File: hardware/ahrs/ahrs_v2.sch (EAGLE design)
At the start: 41 parts, among them J1 LINEAR_2_5040500291, J2 LINEAR_35040500391, J3 LINEAR_85040500891, U1 STM32G4_UFQFPN48_T1, U10 MCP2542FD, U11 LDFM33PUR, U2 LSM9DS1, X1 CRYSTAL_NX2016SA-24MHZ-EXS00A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

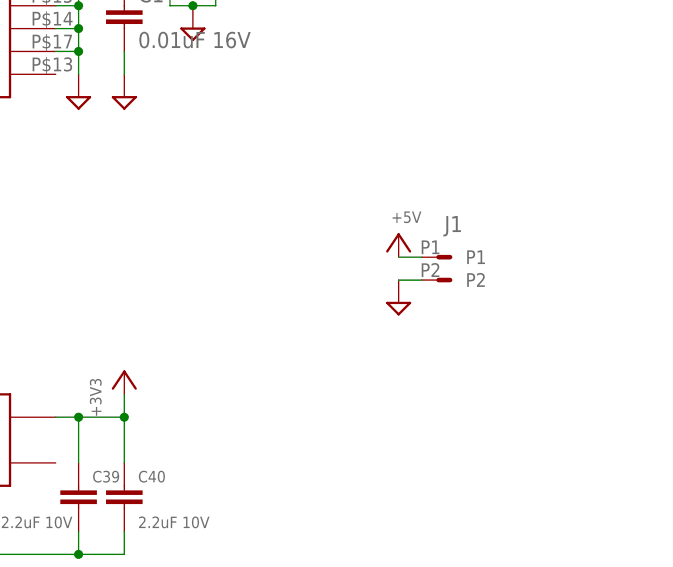
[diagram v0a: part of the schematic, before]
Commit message: Added TVS diode
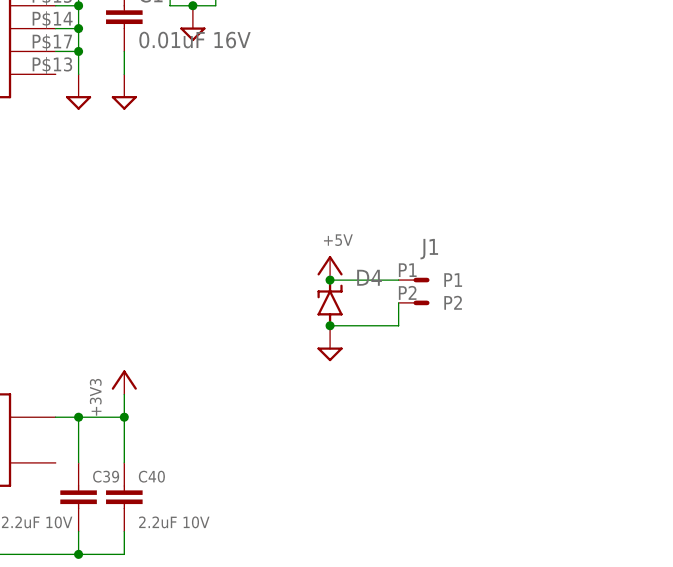
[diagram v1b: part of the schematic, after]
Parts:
- added D4: (no value), _T_rcl:TVS_SOD123
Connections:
- net +5V: now also D4.C
- net GND: now also D4.A
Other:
- moved on the sheet: J1
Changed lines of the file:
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@@
 <part name="R3" library="_T_rcl" library_urn="urn:adsk.eagle:library:19571919" deviceset="R" device="0603" package3d_urn="urn:adsk.eagle:package:19572012/3" value="22"/>
 <part name="GND13" library="_T_power" library_urn="urn:adsk.eagle:library:19572085" deviceset="GND" device=""/>
+<part name="D4" library="_T_rcl" library_urn="urn:adsk.eagle:library:19571919" deviceset="TVS" device="_SOD123" package3d_urn="urn:adsk.eagle:package:20295471/2"/>
 </parts>
 <sheets>
@@
 <attribute name="VALUE" x="70.8406" y="70.0786" size="2.0828" layer="96" ratio="6" rot="SR0"/>
 </instance>
-<instance part="J1" gate="G$1" x="251.46" y="91.44" smashed="yes" grouprefs="POWER">
-<attribute name="NAME" x="248.92" y="94.234" size="1.778" layer="95"/>
-</instance>
-<instance part="GND12" gate="G$1" x="243.84" y="86.36" smashed="yes" grouprefs="POWER"/>
-<instance part="+5V2" gate="G$1" x="243.84" y="93.98" smashed="yes" grouprefs="POWER">
-<attribute name="VALUE" x="246.38" y="96.52" size="1.27" layer="96" rot="R180"/>
+<instance part="J1" gate="G$1" x="248.92" y="88.9" smashed="yes" grouprefs="POWER">
+<attribute name="NAME" x="246.38" y="91.694" size="1.778" layer="95"/>
+</instance>
+<instance part="GND12" gate="G$1" x="236.22" y="81.28" smashed="yes" grouprefs="POWER"/>
+<instance part="+5V2" gate="G$1" x="236.22" y="91.44" smashed="yes" grouprefs="POWER">
+<attribute name="VALUE" x="238.76" y="93.98" size="1.27" layer="96" rot="R180"/>
 </instance>
 <instance part="J3" gate="G$1" x="269.24" y="134.62" smashed="yes" grouprefs="DEBUG">
@@
 </instance>
 <instance part="GND13" gate="G$1" x="154.94" y="10.16" smashed="yes" grouprefs="LED_INFO"/>
+<instance part="D4" gate="G$1" x="236.22" y="86.36" smashed="yes" grouprefs="POWER">
+<attribute name="NAME" x="239.014" y="88.265" size="1.778" layer="95"/>
+<attribute name="VALUE" x="239.014" y="85.471" size="1.778" layer="96"/>
+</instance>
 </instances>
 <busses>
@@
 <pinref part="J1" gate="G$1" pin="P2"/>
 <pinref part="GND12" gate="G$1" pin="GND"/>
-<wire x1="246.38" y1="88.9" x2="243.84" y2="88.9" width="0.1524" layer="91" grouprefs="POWER"/>
+<pinref part="D4" gate="G$1" pin="A"/>
+<junction x="236.22" y="83.82" grouprefs="POWER"/>
+<wire x1="236.22" y1="83.82" x2="243.84" y2="83.82" width="0.1524" layer="91" grouprefs="POWER"/>
+<wire x1="243.84" y1="83.82" x2="243.84" y2="86.36" width="0.1524" layer="91" grouprefs="POWER"/>
 </segment>
 <segment>
@@
 <pinref part="J1" gate="G$1" pin="P1"/>
 <pinref part="+5V2" gate="G$1" pin="+5V"/>
-<wire x1="246.38" y1="91.44" x2="243.84" y2="91.44" width="0.1524" layer="91" grouprefs="POWER"/>
-</segment>
-</net>
+<wire x1="243.84" y1="88.9" x2="236.22" y2="88.9" width="0.1524" layer="91" grouprefs="POWER"/>
+<pinref part="D4" gate="G$1" pin="C"/>
+<junction x="236.22" y="88.9" grouprefs="POWER"/>
+</segment>
+</net>
